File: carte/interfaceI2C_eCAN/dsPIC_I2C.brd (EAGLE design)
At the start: 59.8 x 40.9 mm, 54 parts, among them IC2 DSPIC33FJ128MC804PT, J1 RJ11-2L-B, J9 22-27-2051, Q2 BSS123, Q4 BSS123, U2 LP2985-33DBVR

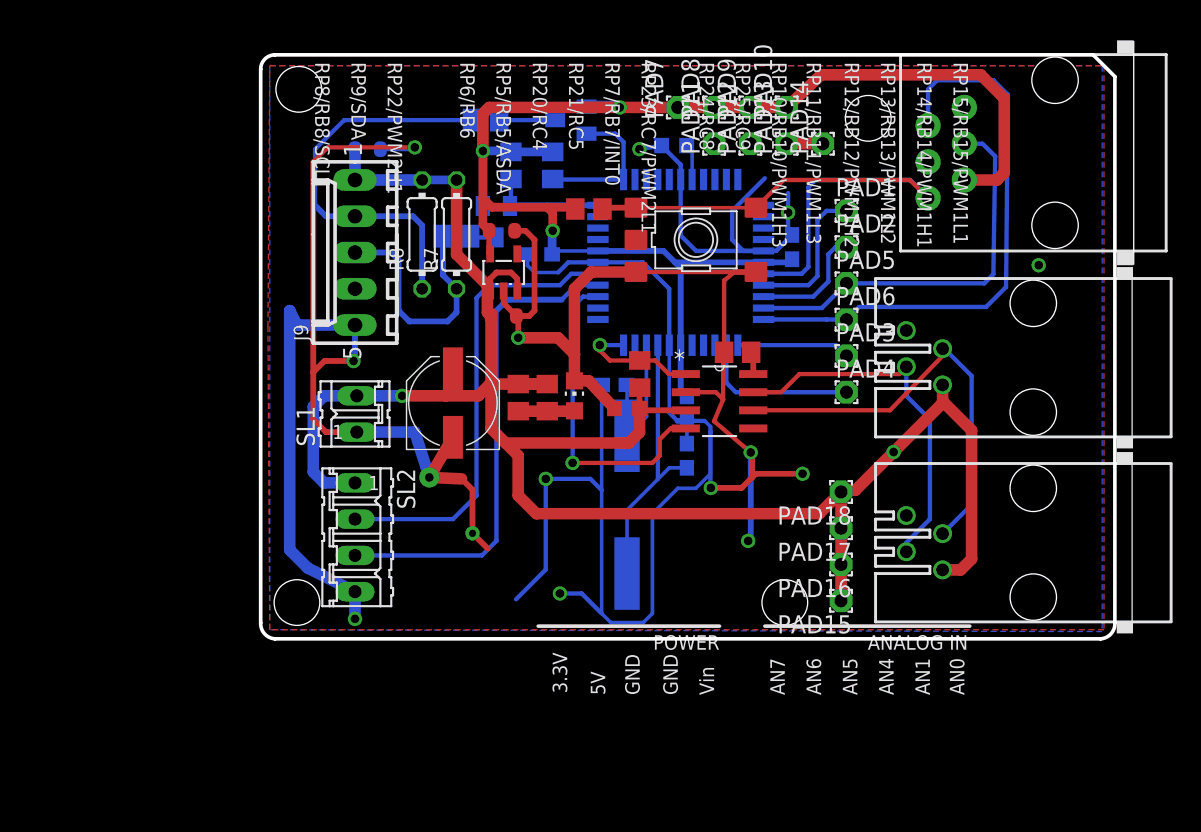
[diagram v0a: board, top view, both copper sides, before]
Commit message: update dsPIC_I2C
Petite mise en forme des sch et brd
rajout d'un README
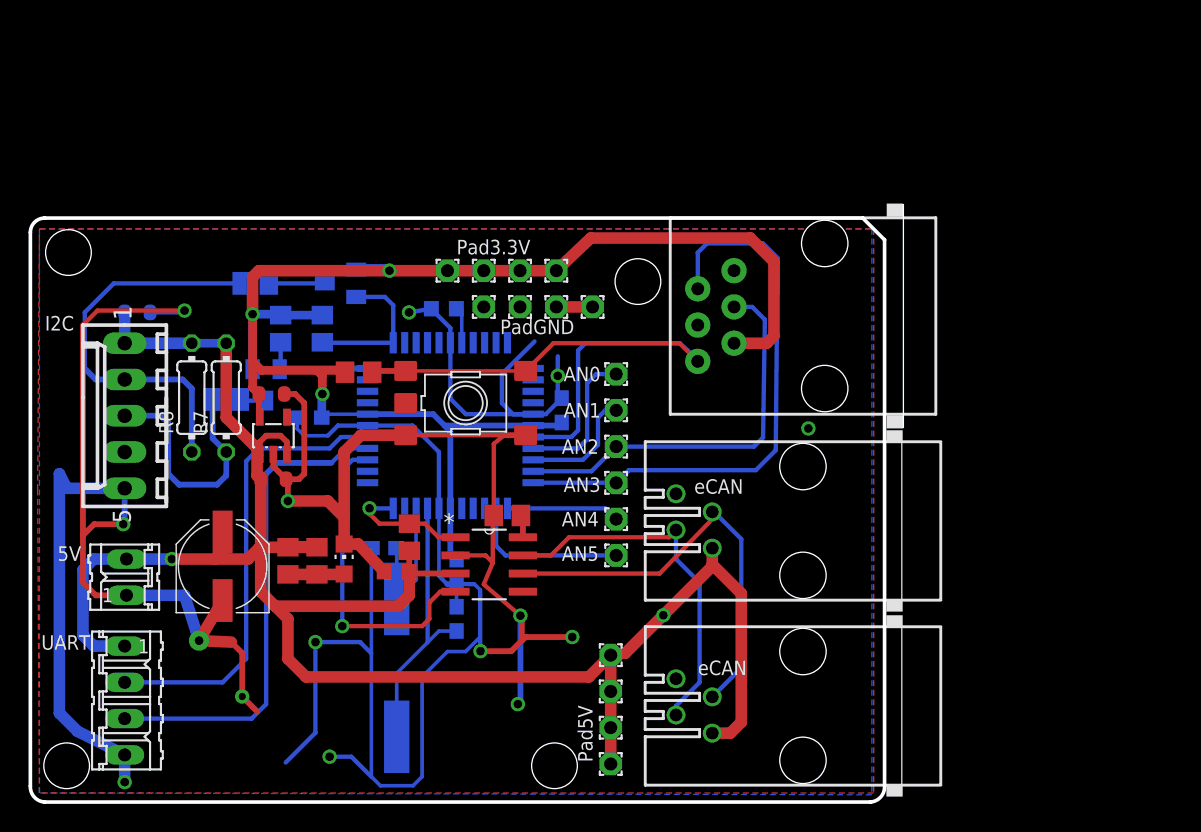
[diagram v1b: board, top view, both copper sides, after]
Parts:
- moved J1 19.8 mm to (53.1, 31.5)
- moved C2 19.8 mm to (4.95, 31.8)
- moved C4 19.8 mm to (26.4, 32.0)
- moved FERRITE2 19.8 mm to (13.2, 33.8)
- moved IC2 19.8 mm to (26.9, 23.8)
- moved J2 19.8 mm to (51.6, 17.1)
- moved J3 19.8 mm to (51.6, 4.19)
- moved J9 19.8 mm to (4.06, 24.5)
- moved ON 19.8 mm to (19.4, 14.5)
- moved PAD14 19.8 mm to (36.8, 32.1)
- moved Q1 19.8 mm to (23.1, 6.86)
- moved Q4 19.8 mm to (19.2, 33.8)
- moved R2 19.8 mm to (30.9, 17.5)
- moved R9 19.8 mm to (17.9, 30.6)
- moved RESET 19.8 mm to (27.9, 25.4)
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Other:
- board text added: "AN2"
- board text added: "AN3"
- board text added: "I2C"
- board text added: "Pad3.3V"
- board text added: "Pad5V"
- board text added: "PadGND"
- board text added: "UART"
- board text added: "eCAN"
- board text removed: "AN6"
- board text removed: "AN7"
- board text removed: "ANALOG IN"
- board text removed: "POWER"
- board text removed: "RP10/RB10/PWM1H3"
- board text removed: "RP22/PWM2H1"
- board text removed: "RP23/RC7/PWM2L1"
- board text removed: "RP24/RC8"
- board text removed: "RP25/RC9"
- board text removed: "RP6/RB6"
- board text removed: "RP7/RB7/INT0"
- board text removed: "RP9/SDA"
